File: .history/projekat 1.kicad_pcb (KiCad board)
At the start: 2 copper layers, 221 parts, among them J1 Keyer, J2 audio_input, J3 Output signal, K1 Relay_SPST-NO_SSB (G6B-1177C(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, K2 Relay_SPST-NO_CW (G6B-1177C(-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, Q1 BC547, Q2 BC547, Q3 BC549, Q4 BC549, Q5 BC549, Q6 BC547, Q7 IRF510, Q9 BC547, SW1 on/off_12V, SW3 audio_SsbMorse_selektor, SW4 on/off_zujanje, SW5 keying_CW_SSB_selektor, SW6 selektor_modulacija, SW7 selektor_izlaza, U1 LM386, U10 OPA656UB, U11 L7806, U12 LM386, U13 OPA656UB, U14 OPA656UB, U15 OPA656UB, U2 LM358, U3 LM358, U4 LM358, U5 OPA656UB, U6 4N35, U7 OPA656UB, U8 OPA656UB, U9 OPA656UB

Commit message: rešen problem errora na pcb-u, replicirati rešenjesa J1 konektora na svim ostalim simbolima koji zadaju error.
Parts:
- added J1: Conn_01x02_Pin, Connector_PinHeader_2.54mm:PinHeader_1x02_P2.54mm_Vertical, F.Cu at (96.5, 124.2)
- added var_att_300mVrms2: 100k linear pot, Potentiometer_THT:Potentiometer_Bourns_3386W_Horizontal, F.Cu at (103.5, 125.5)
- MC1496_mix2, MC1496_mod1: footprint Package_SO:SOIC-14-16_3.9x9.9mm_P1.27mm -> Package_SO:SOIC-14_3.9x8.7mm_P1.27mm
- moved L2 163.1 mm to (165.7, 31.7)
- moved MC1496_mix2 162.0 mm to (156.0, 48.5)
- moved carrier_null_2 155.1 mm to (124.1, 28.0)
- moved RFC_3 154.6 mm to (166.1, 38.9)
- moved RFC_4 154.6 mm to (166.1, 42.3)
- moved R21 137.2 mm to (180.2, 17.2)
- moved R22 137.2 mm to (180.2, 20.5)
- moved R23 137.2 mm to (180.2, 23.8)
- moved R24 137.2 mm to (180.2, 27.1)
- moved R25 137.2 mm to (180.2, 30.4)
- moved R27 137.2 mm to (180.2, 37.0)
- moved R28 137.2 mm to (180.2, 40.3)
- moved R29 137.2 mm to (180.2, 43.7)
- moved R30 137.2 mm to (180.2, 47.0)
- moved R26 137.2 mm to (180.2, 33.7)
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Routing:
- net Net-(C42-Pad1): track 11.7 -> 5.24 mm
- net Net-(U14-NEG): track 15.8 -> 13.0 mm
- net GND: track 0.00 -> 2.00 mm
- net Net-(C42-Pad2): track 3.45 -> 2.16 mm
- net /output_amplification_cw: track 8.62 -> 7.53 mm
- net Net-(C41-Pad2): track 2.95 -> 1.95 mm
- net Net-(C41-Pad1): track 8.88 -> 7.91 mm

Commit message: organizovan layout tone generation, signal input, headphone interface. Promenjen net na LE diodi u 12V_supply_1 i dodat otpornik od 500 oma.
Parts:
- removed the J1 at (96.0, 107.0)
- removed TS_6.35mm1: head_out, Connector_PinHeader_2.54mm:PinHeader_1x01_P2.54mm_Vertical
- added J4: Conn_01x02_Pin, Connector_PinHeader_2.54mm:PinHeader_1x02_P2.54mm_Vertical, F.Cu at (314.3, 278.0)
- added R63: 500, Resistor_SMD:R_1206_3216Metric_Pad1.30x1.75mm_HandSolder, F.Cu at (269.7, 237.5)
- BZ1: footprint Connector_PinHeader_2.54mm:PinHeader_1x01_P2.54mm_Vertical -> Connector_PinHeader_2.54mm:PinHeader_1x02_P2.54mm_Vertical
- J2: value audio_input -> Conn_01x02_Pin
- R62: footprint Package_TO_SOT_THT:TO-220-3_Vertical -> Resistor_THT:R_Axial_DIN0516_L15.5mm_D5.0mm_P20.32mm_Horizontal
- SW4: footprint Connector_PinHeader_2.54mm:PinHeader_1x01_P2.54mm_Vertical -> Connector_PinHeader_2.54mm:PinHeader_1x03_P2.54mm_Vertical
- moved C38 322.2 mm to (318.5, 277.5)
- moved C30 312.6 mm to (301.0, 262.0)
- moved C_audio_coupling1 311.1 mm to (321.0, 263.5), turned to 180 degrees
- moved C29 310.2 mm to (301.0, 254.0), turned to 180 degrees
- moved C31 305.4 mm to (301.0, 251.0)
- moved C33 298.1 mm to (305.0, 233.5)
- moved C27 294.3 mm to (293.5, 260.5), turned to -90 degrees
- moved C34 293.6 mm to (305.0, 225.5)
- moved C32 291.2 mm to (290.5, 244.0), turned to -90 degrees
- moved C28 281.6 mm to (280.5, 261.5), turned to -90 degrees
- moved C35 281.6 mm to (291.0, 231.0), turned to -90 degrees
- moved R_head1 277.2 mm to (299.4, 227.0), turned to -90 degrees
- moved SW3 275.0 mm to (311.0, 263.0), turned to 90 degrees
- moved R46 271.4 mm to (309.0, 246.0), turned to -90 degrees
- moved R45 271.1 mm to (306.5, 246.0), turned to -90 degrees
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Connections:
- C37 pad 2: Net-(C37-Pad2) -> Net-(J2-Pin_2)
- D1 pad 2: VCC -> Net-(D1-A)
- J2 pad 1: (no net) -> GND
- J2 pad 2: (no net) -> Net-(J2-Pin_2)
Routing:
- net /12V_supply_1: track 20.0 -> 140.4 mm
- net Net-(Q3-C): track 0.00 -> 31.2 mm
- net Net-(U4B--): track 0.00 -> 23.7 mm
- net Net-(U2A-+): track 0.00 -> 23.3 mm
- net Net-(C31-Pad1): track 0.00 -> 21.9 mm
- net Net-(SW3-A): track 0.00 -> 19.8 mm
- net Net-(Q3-E): track 0.00 -> 14.4 mm
- net Net-(U2B--): track 0.00 -> 14.1 mm
- net +6V: track 0.00 -> 13.4 mm
- net Net-(U2A--): track 0.00 -> 12.5 mm
- net Net-(R40-Pad2): track 0.00 -> 11.5 mm
- net Net-(C27-Pad1): track 0.00 -> 9.76 mm
- net Net-(Q4-B): track 0.00 -> 9.07 mm
- net Net-(SW5-A): track 0.00 -> 8.45 mm
- net Net-(U3A-+): track 0.00 -> 8.33 mm
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
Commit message: Izvršena prva korekcija layout-a tone generation, signal input, headphone interfacebloka, zamenjen footprint lm358 u SOIC-8. U sledećoj iteraciji dodati više slojeva, trace-ve koji su ispod komponenata spustiti u donji sloj, pregledati trace-ove
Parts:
- R63: value 500 -> 220
- U2, U3, U4: footprint Package_DIP:DIP-8_W7.62mm_LongPads -> Package_SO:SOIC-8_3.9x4.9mm_P1.27mm
- moved decoup_+6V1 244.2 mm to (266.0, 238.5), turned to 180 degrees
- moved U11 210.8 mm to (263.5, 232.9)
- moved J4 20.4 mm to (314.9, 257.6), turned to 180 degrees
- moved U12 16.7 mm to (318.6, 258.1), turned to 0 degrees
- moved C38 15.9 mm to (315.4, 261.9), turned to -90 degrees
- moved C_audio_coupling1 6.56 mm to (315.4, 266.9), turned to 90 degrees
- moved SW3 6.03 mm to (308.5, 257.5), turned to 0 degrees
- moved U2 5.37 mm to (287.5, 260.5)
- moved R46 4.09 mm to (308.0, 242.0), turned to 0 degrees
- moved U3 3.10 mm to (308.5, 253.0)
- moved U4 2.66 mm to (311.5, 230.0)
- moved C36 1.50 mm to (274.0, 228.5)
- moved C37 1.50 mm to (276.5, 228.5)
- moved J2 1.50 mm to (273.7, 233.0)
- moved U1 1.50 mm to (286.8, 234.8)
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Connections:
- R63 pad 1: /12V_supply_1 -> +6V
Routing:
- net /12V_supply_1: track 140.4 -> 173.4 mm
- net Net-(U2B--): track 14.1 -> 4.58 mm
- net Net-(C_audio_coupling1-Pad1): track 3.26 -> 11.9 mm
- net +6V: track 13.4 -> 21.9 mm
- net Net-(SW3-A): track 19.8 -> 13.8 mm
- net Net-(SW3-C): track 3.69 -> 8.03 mm
- net Net-(U2A-+): track 23.3 -> 27.5 mm
- net Net-(U4B--): track 23.7 -> 19.5 mm
- net Net-(C31-Pad1): track 21.9 -> 17.9 mm
- net Net-(U3A-+): track 8.33 -> 12.0 mm
- net Net-(R40-Pad2): track 11.5 -> 15.0 mm
- net Net-(Q3-B): track 6.75 -> 4.35 mm
- net Net-(SW3-B): track 3.77 -> 6.16 mm
- net Net-(U1-+): track 2.77 -> 4.56 mm
- net Net-(U4B-+): track 6.32 -> 4.74 mm
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
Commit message: dorađen layout pcb-a, dodati novi layeri, sprovedene vije.
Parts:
- PWR_1, SW1: footprint Connector_PinHeader_2.54mm:PinHeader_1x01_P2.54mm_Vertical -> Connector_PinHeader_2.54mm:PinHeader_1x02_P2.54mm_Vertical
- moved K1 587.0 mm to (652.7, -5.61)
- moved K2 587.0 mm to (664.3, -5.61)
- moved SW7 587.0 mm to (666.5, -74.5)
- moved C39 308.6 mm to (545.0, -20.0)
- moved C40 308.6 mm to (543.5, -8.47)
- moved C_d_op_2_2 308.6 mm to (559.0, 39.5)
- moved L10 308.6 mm to (564.0, -54.5)
- moved L11 308.6 mm to (568.1, -56.0)
- moved L5 308.6 mm to (573.9, -73.0)
- moved L6 308.6 mm to (569.4, -71.5)
- moved R56 308.6 mm to (575.4, -67.0)
- moved R58 308.6 mm to (552.0, -20.0)
- moved R59 308.6 mm to (555.0, -11.0)
- moved R60 308.6 mm to (550.5, -10.5)
- moved R_filter_2 308.6 mm to (559.0, 43.0)
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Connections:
- R_bleed_12V1 pad 1: VCC -> /12V_supply_1
- VCC_decoup_12v1 pad 1: VCC -> /12V_supply_1
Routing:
- net /12V_supply_1: track 173.4 -> 61.6 mm, vias 0 -> 25
- net GND: track 2.00 -> 106.2 mm, vias 44 -> 62
- net /1k_820_junction: track 0.00 -> 39.9 mm, vias 0 -> 2
- net /4: track 0.00 -> 37.1 mm, vias 0 -> 3
- net /1k_820_junction_2: track 0.00 -> 34.4 mm, vias 0 -> 3
- net /4_2: track 0.00 -> 27.2 mm, vias 0 -> 3
- net Net-(C11-Pad2): track 0.00 -> 26.6 mm, vias 0 -> 2
- net /buff_02: track 39.8 -> 17.7 mm
- net Net-(C18-Pad2): track 0.00 -> 21.6 mm, vias 0 -> 2
- net /buff_01: track 36.5 -> 15.4 mm, vias 0 -> 2
- net Net-(R16-Pad2): track 0.00 -> 18.0 mm
- net Net-(CP3_2-Pad1): track 0.00 -> 17.9 mm, vias 0 -> 2
- net Net-(R19-Pad2): track 0.00 -> 17.6 mm
- net Net-(C12-Pad2): track 0.00 -> 16.4 mm, vias 0 -> 2
- net Net-(CS2-Pad1): track 0.00 -> 16.2 mm, vias 0 -> 2
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- added copper zone on F.Cu, net (none)
- added copper zone on B.Cu, net /12V_supply_1
- added copper zone on In1.Cu, net GND
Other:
- board outline added: 100 x 100 mm
- copper layers 2 -> 4

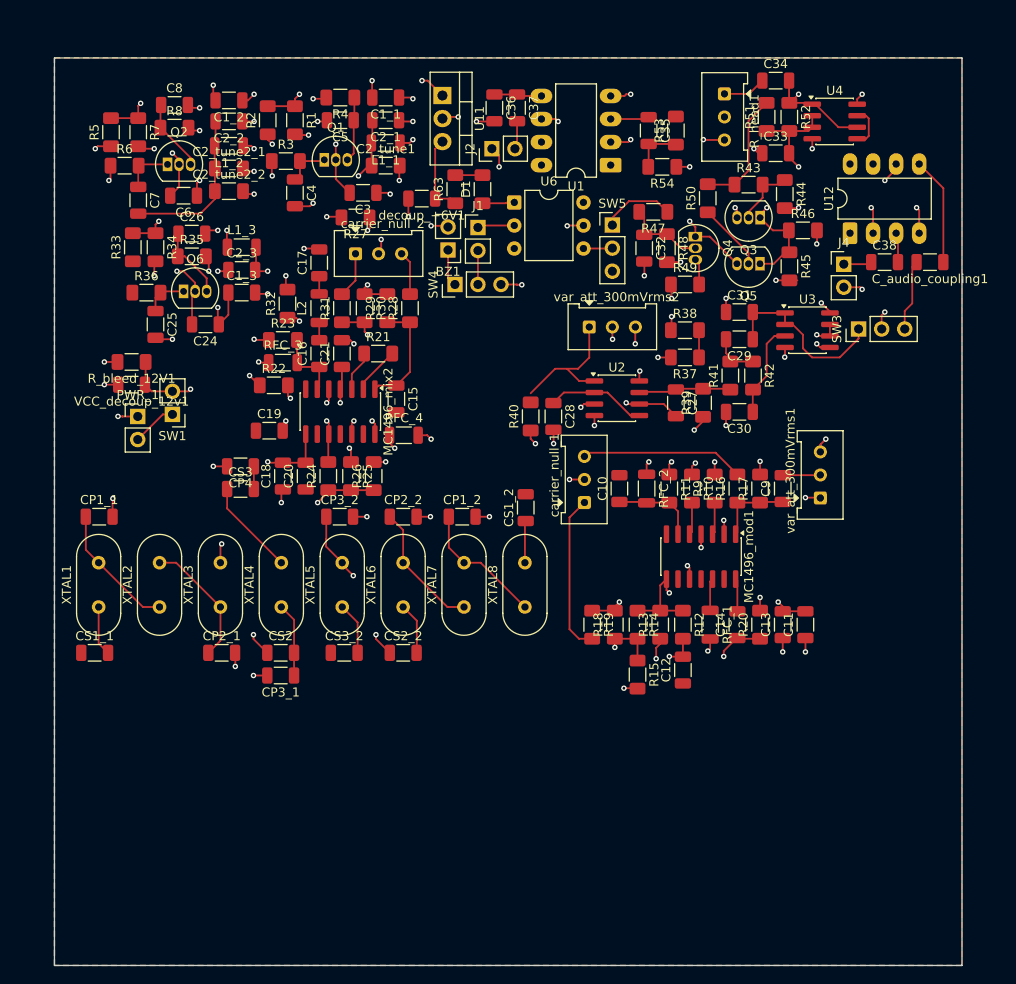
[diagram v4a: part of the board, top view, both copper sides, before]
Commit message: Dodati decoupling koncdnzatori na sve blokove i operacione, obrisan gornji layer bakra, sve vije prebačene na through, drc zadaje erore da su netovi šortivani
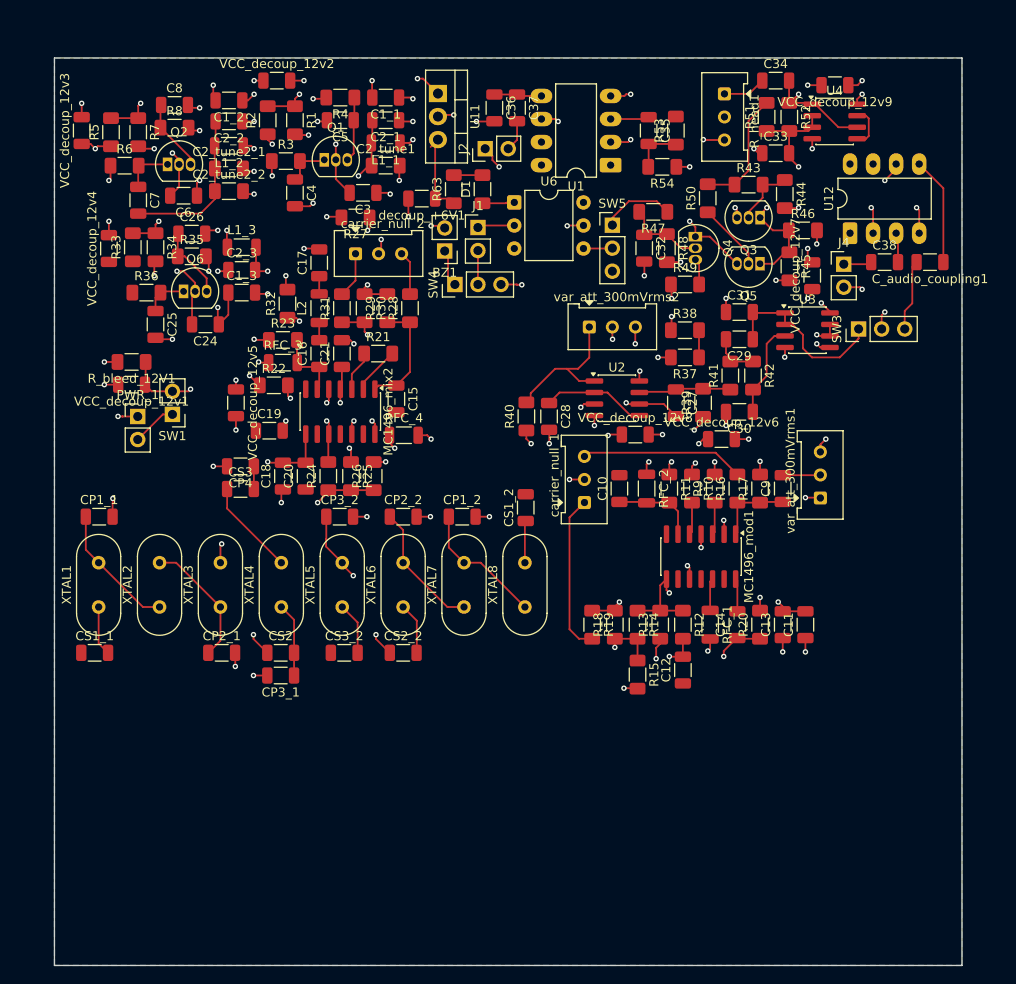
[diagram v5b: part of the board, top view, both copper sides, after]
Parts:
- added VCC_decoup_12v2: 100n, Capacitor_SMD:C_1206_3216Metric, F.Cu at (124.5, 52.5)
- added VCC_decoup_12v3: 100n, Capacitor_SMD:C_1206_3216Metric, F.Cu at (103.0, 58.0)
- added VCC_decoup_12v4: 100n, Capacitor_SMD:C_1206_3216Metric, F.Cu at (106.0, 71.0)
- added VCC_decoup_12v5: 100n, Capacitor_SMD:C_1206_3216Metric, F.Cu at (120.0, 88.0)
- added VCC_decoup_12v6: 100n, Capacitor_SMD:C_1206_3216Metric, F.Cu at (173.5, 92.0)
- added VCC_decoup_12v7: 100n, Capacitor_SMD:C_1206_3216Metric, F.Cu at (183.5, 74.0)
- added VCC_decoup_12v8: 100n, Capacitor_SMD:C_1206_3216Metric, F.Cu at (164.0, 91.5)
- added VCC_decoup_12v9: 100n, Capacitor_SMD:C_1206_3216Metric, F.Cu at (186.0, 53.0)
- moved J2 0.74 mm to (147.5, 60.0)
- moved U11 0.55 mm to (142.3, 53.9)
- moved C28 0.47 mm to (154.5, 89.5)
- moved R40 0.47 mm to (152.0, 89.5)
- moved BZ1 0.39 mm to (143.0, 71.3)
- moved R63 0.16 mm to (144.0, 64.5)
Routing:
- net GND: track 106.2 -> 118.6 mm, vias 62 -> 70
- net /12V_supply_1: track 61.6 -> 71.1 mm, vias 25 -> 31
- net Net-(R40-Pad2): track 15.0 -> 16.2 mm
- removed copper zone on F.Cu, net (none)

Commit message: dodati footprinti za promenljive kondenzatore (proveriti da li su adekvatni)
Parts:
- removed C1, C2, C41, C42: 100p, Capacitor_SMD:C_1206_3216Metric
- removed C39, C40, decoup_+6V1: 100n, Capacitor_SMD:C_1206_3216Metric
- removed C_d_op1, C_d_op2, C_d_op3, C_d_op4, C_d_op5: 0,1u, Capacitor_SMD:C_1206_3216Metric
- removed C_d_op_2_1, C_d_op_2_2: 10n, Capacitor_SMD:C_1206_3216Metric
- removed C_dc1, C_dc2, C_lo_vfo1: 10nF, Capacitor_SMD:C_1206_3216Metric
- removed J3: Output signal, Connector_PinHeader_2.54mm:PinHeader_1x02_P2.54mm_Vertical
- removed K1: Relay_SPST-NO_SSB (G6B-1177C(-FD)-ND-US), footprints:RELAY_G6B-1177P-ND_OMR
- removed K2: Relay_SPST-NO_CW (G6B-1177C(-FD)-ND-US), footprints:RELAY_G6B-1177P-ND_OMR
- removed L1, L11, L5, L7: 1.6u, Inductor_SMD:L_1206_3216Metric
- removed L10, L3, L6, L8: 3.9u, Inductor_SMD:L_1206_3216Metric
- removed L4, L9: 750n, Capacitor_SMD:C_1206_3216Metric
- removed Q7: IRF510, Package_TO_SOT_THT:TO-220-3_Vertical
- removed Q9: BC547, Package_TO_SOT_THT:TO-92_Inline
- removed R55, R56, R61: 50R, Package_TO_SOT_THT:TO-220-3_Vertical
- removed R57: R, Package_TO_SOT_THT:TO-220-3_Vertical
- removed R58, R59, R60, R_f3, R_filter_1, R_filter_2, R_in3: R, Resistor_SMD:R_1206_3216Metric_Pad1.30x1.75mm_HandSolder
- removed R62: 50R, Resistor_THT:R_Axial_DIN0516_L15.5mm_D5.0mm_P20.32mm_Horizontal
- removed RV1: 100k, Resistor_SMD:R_1206_3216Metric_Pad1.30x1.75mm_HandSolder
- removed R_f1: 127k, Resistor_SMD:R_1206_3216Metric_Pad1.30x1.75mm_HandSolder
- removed R_f2: 3k, Resistor_SMD:R_1206_3216Metric_Pad1.30x1.75mm_HandSolder
- removed R_in1: 1k, Package_TO_SOT_THT:TO-220-3_Vertical
- removed R_in2: 1k, Resistor_SMD:R_1206_3216Metric_Pad1.30x1.75mm_HandSolder
- removed SW6: selektor_modulacija, Connector_PinHeader_2.54mm:PinHeader_1x03_P2.54mm_Vertical
- removed SW7: selektor_izlaza, Connector_PinHeader_2.54mm:PinHeader_1x03_P2.54mm_Vertical
- removed U10, U13, U14, U15, U5, U7, U8, U9: OPA656UB, Package_SO:SOIC-8-1EP_3.9x4.9mm_P1.27mm_EP2.95x4.9mm_Mask2.34x2.34mm
- removed U11: L7806, Package_TO_SOT_THT:TO-220-3_Vertical
- removed var_att1, var_att_100mVrms1, var_att_15mVrms1, var_att_60mVrms1: 1k linear pot, Potentiometer_THT:Potentiometer_Bourns_3386W_Horizontal
- added C22: 10-60pF, Capacitor_SMD:C_Trimmer_Voltronics_JZ, F.Cu at (125.0, 77.8)
- added C23: 10-60pF, Capacitor_SMD:C_Trimmer_Voltronics_JZ, F.Cu at (125.0, 73.5)
- added C2_tune3: 5-30p, Capacitor_SMD:C_Trimmer_Voltronics_JZ, F.Cu at (124.7, 69.4)
- added SW2: SW_Nidec_CAS-120A1, Connector_PinHeader_2.54mm:PinHeader_1x03_P2.54mm_Vertical, F.Cu at (103.5, 122.2)
- C2_tune1, C2_tune2_1, C2_tune2_2: footprint Resistor_SMD:R_1206_3216Metric_Pad1.30x1.75mm_HandSolder -> Capacitor_SMD:C_Trimmer_Voltronics_JZ
- moved VCC_decoup_12v6 25.5 mm to (174.5, 117.5)
- moved VCC_decoup_12v8 8.76 mm to (168.5, 84.0)
- moved R32 7.20 mm to (120.0, 81.5)
- moved C3 2.98 mm to (131.0, 65.0)
- moved C1_2 2.18 mm to (119.2, 52.5)
- moved C2_2 2.18 mm to (119.2, 54.8)
- moved L1_2 2.18 mm to (119.2, 57.5)
- moved C1_3 1.66 mm to (119.0, 75.9)
- moved C24 1.66 mm to (115.0, 79.4)
- moved C25 1.66 mm to (109.5, 79.4)
- moved C26 1.66 mm to (113.5, 69.4)
- moved C2_3 1.66 mm to (119.0, 73.4)
- moved L1_3 1.66 mm to (119.0, 70.9)
- moved Q6 1.66 mm to (112.6, 75.7)
- moved R33 1.66 mm to (107.0, 70.9)
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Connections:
- R2 pad 1: /12V_supply_1 -> /12V_supply_2
- R3 pad 1: /12V_supply_1 -> /12V_supply_2
- R5 pad 1: /12V_supply_1 -> /12V_supply_2
- R6 pad 1: /12V_supply_1 -> /12V_supply_2
- VCC_decoup_12v2 pad 1: /12V_supply_1 -> /12V_supply_2
- VCC_decoup_12v3 pad 1: /12V_supply_1 -> /12V_supply_2
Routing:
- net /12V_supply_2: track 0.00 -> 106.7 mm, vias 0 -> 5
- net /12V_supply_CW: track 2.59 -> 55.7 mm, vias 0 -> 1
- net Net-(U8-NEG): track 40.7 -> 0.00 mm
- net Net-(U7-NEG): track 37.8 -> 0.00 mm
- net Net-(U5-NEG): track 36.1 -> 0.00 mm
- net +6V: track 22.7 -> 53.4 mm, vias 0 -> 2
- net Net-(U10-NEG): track 26.7 -> 0.00 mm
- net /2nd_ampl: track 25.4 -> 0.00 mm
- net Net-(Q7-D): track 22.2 -> 0.00 mm
- net Net-(CP4-Pad1): track 2.50 -> 24.3 mm, vias 0 -> 2
- net Net-(Q9-C): track 17.6 -> 0.00 mm
- net Net-(U13-OUTPUT): track 17.6 -> 0.00 mm
- net Net-(U13-NEG): track 16.0 -> 0.00 mm
- net Net-(U14-NEG): track 13.0 -> 0.00 mm
- net /12V_supply_1: track 71.1 -> 58.3 mm, vias 31 -> 24
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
